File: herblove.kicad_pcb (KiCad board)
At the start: 2 copper layers, 56 x 51 mm, 18 parts, among them J1 Conn_01x01_Pin, J2 12V Valve, J3 Empty Sensor, J4 Switched Battery, J5 Solar Panel, J6 Micro_SD_Card, J7 Conn_01x04_Pin, SW1 SW_Push, SW2 SW_SPDT, SW3 SW_Push, U1 bme280, U2 C3 Pico, U3 hw357

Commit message: Ground all the negative terminals of the battery step up converter
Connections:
- BT1 pad 2: Net-(BT1--) -> GND
- U3 pad 4: unconnected-(U3-O--Pad4) -> GND
- U3 pad 6: Net-(BT1--) -> GND
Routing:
- net GND: track 134.5 -> 144.9 mm
- net Net-(BT1--): track 10.3 -> 0.00 mm

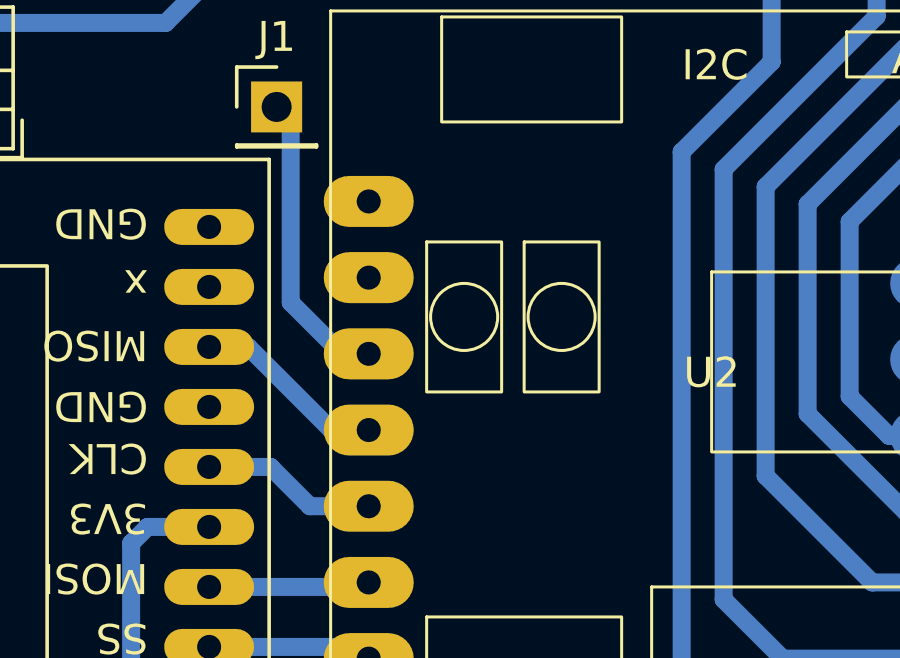
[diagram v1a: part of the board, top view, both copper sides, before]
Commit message: Add a weak pull down for the enable pin of the step up converter
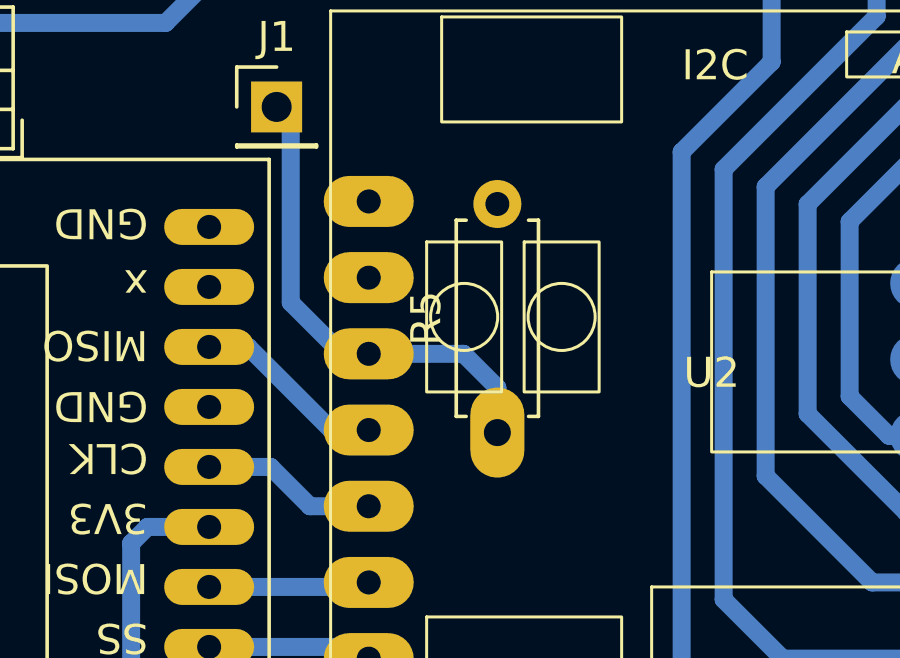
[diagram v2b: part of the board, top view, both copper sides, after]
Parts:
- added R5: 200k, Resistor_THT:R_Axial_DIN0207_L6.3mm_D2.5mm_P7.62mm_Horizontal, F.Cu at (96.4, 107.9)
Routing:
- net ENABLE_12V: track 10.0 -> 16.3 mm

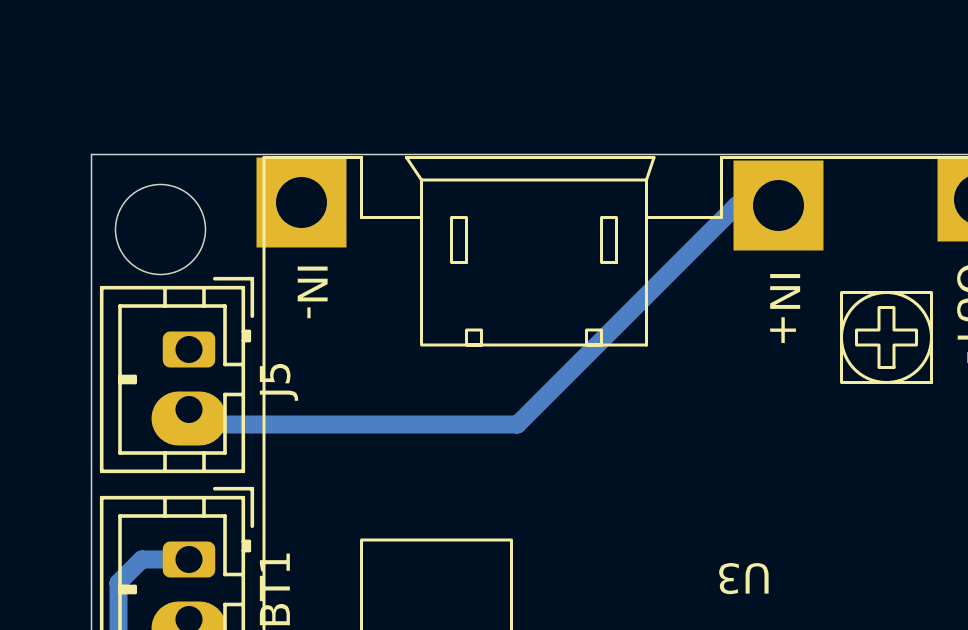
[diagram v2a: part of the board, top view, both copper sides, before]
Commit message: Fix polarity of the solar plug
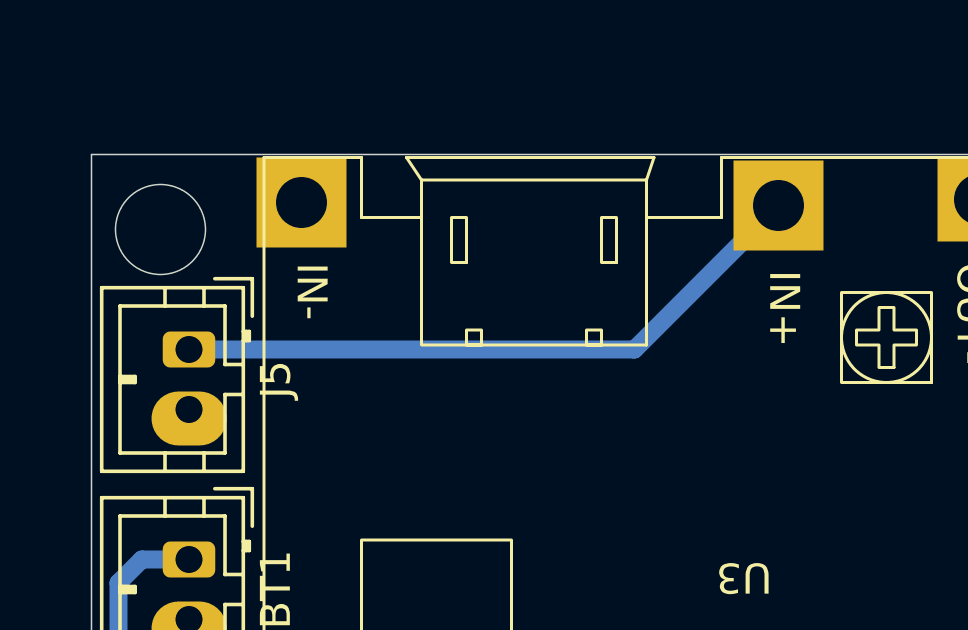
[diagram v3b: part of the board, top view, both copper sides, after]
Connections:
- J5 pad 1: GND -> Net-(J5-Pin_1)
- J5 pad 2: Net-(J5-Pin_2) -> GND
- U3 pad 1: Net-(J5-Pin_2) -> Net-(J5-Pin_1)
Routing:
- net Net-(J5-Pin_2): track 22.9 -> 0.00 mm
- net Net-(J5-Pin_1): track 0.00 -> 21.6 mm
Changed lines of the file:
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@@
 	(net 14 "EMPTY_SENSOR")
 	(net 15 "Net-(J4-Pin_2)")
-	(net 16 "Net-(J5-Pin_2)")
+	(net 16 "Net-(J5-Pin_1)")
 	(net 17 "SWITCH_A")
 	(net 18 "SWITCH_B")
@@
 			(remove_unused_layers no)
 			(roundrect_rratio 0.208333)
-			(net 12 "GND")
+			(net 16 "Net-(J5-Pin_1)")
 			(pinfunction "Pin_1")
 			(pintype "passive")
@@
 			(layers "*.Cu" "*.Mask")
 			(remove_unused_layers no)
-			(net 16 "Net-(J5-Pin_2)")
+			(net 12 "GND")
 			(pinfunction "Pin_2")
 			(pintype "passive")
@@
 			(layers "*.Cu" "*.Mask")
 			(remove_unused_layers no)
-			(net 16 "Net-(J5-Pin_2)")
+			(net 16 "Net-(J5-Pin_1)")
 			(pinfunction "IN+")
 			(pintype "power_in")
@@
 	)
 	(segment
-		(start 71.75 78.5)
-		(end 82.2 78.5)
-		(width 0.6)
-		(layer "B.Cu")
-		(net 16)
-	)
-	(segment
-		(start 89.5 71.2)
+		(start 86.1 76)
 		(end 90.9 71.2)
 		(width 0.6)
@@
 	)
 	(segment
-		(start 82.2 78.5)
-		(end 89.5 71.2)
-		(width 0.6)
-		(layer "B.Cu")
-		(net 16)
-	)
-	(segment
-		(start 71.25 78)
-		(end 71.75 78.5)
+		(start 71.25 76)
+		(end 86.1 76)
 		(width 0.6)
 		(layer "B.Cu")
